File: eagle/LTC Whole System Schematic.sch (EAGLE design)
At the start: 22 parts

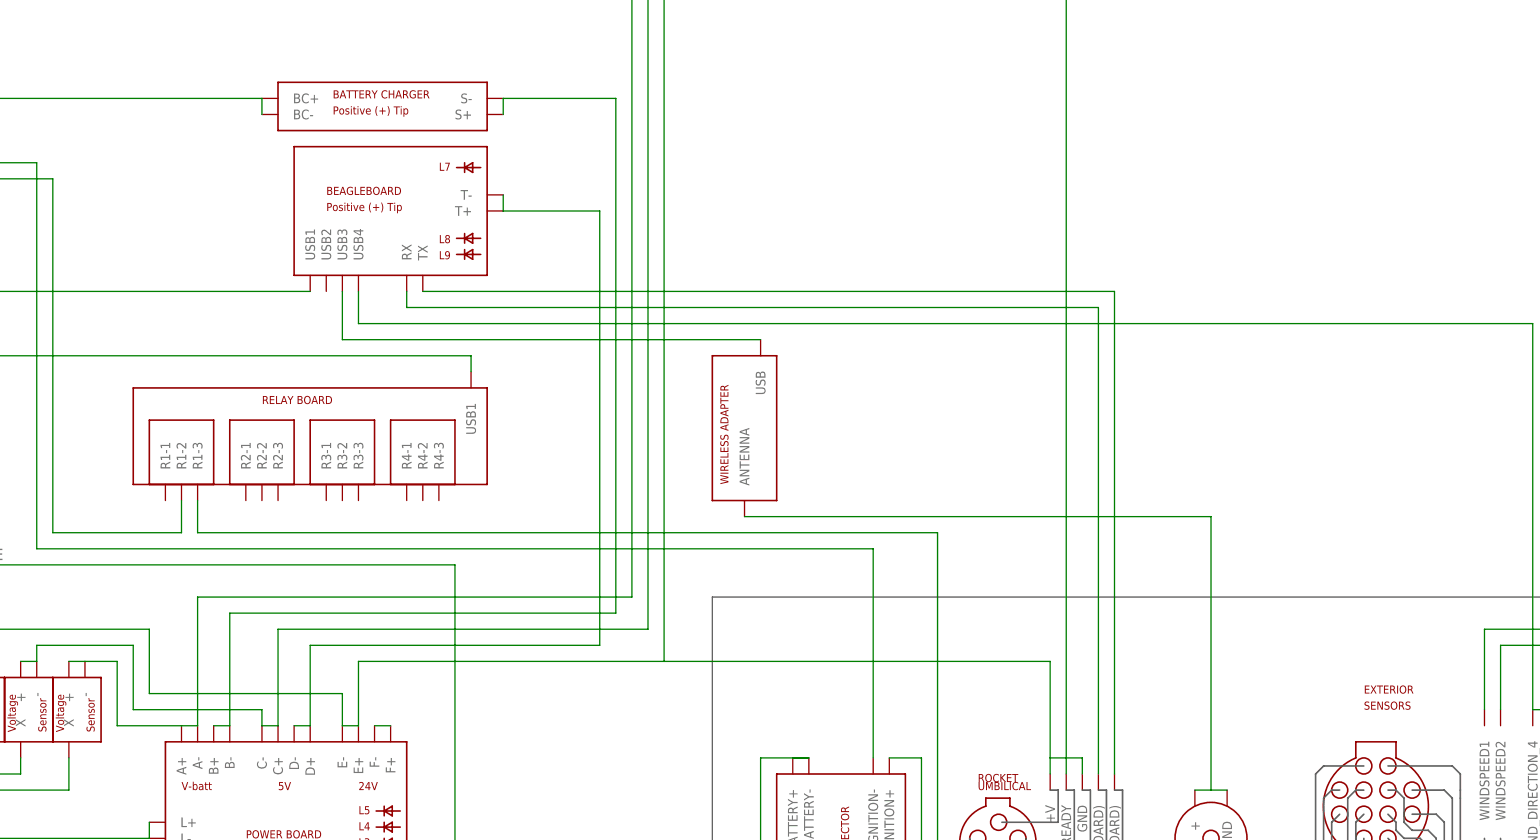
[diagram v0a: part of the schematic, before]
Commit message: Updated LV2 system schematic to include DC-DC adapter and extra relay connections.
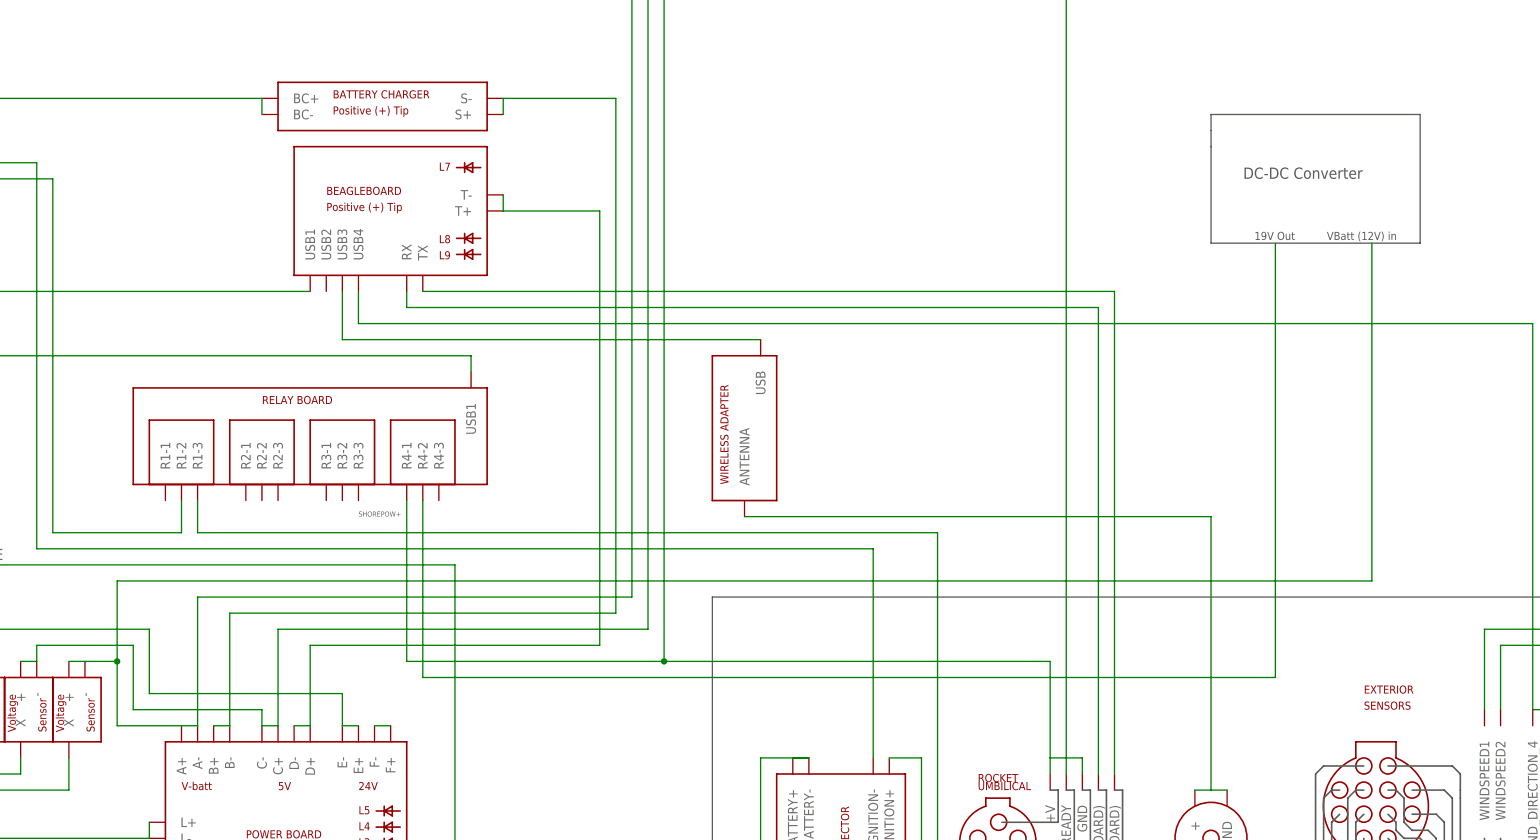
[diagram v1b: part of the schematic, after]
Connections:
- new net N$11: U$1.E+, U$1.E-, U$10.+, U$10.-
- new net SHOREPOW+: U$14.+V, U$14.GND, U$2.R+, U$6.R4-1
- net N$6: now also U$6.R4-2; no longer U$1.E+, U$1.E-, U$10.+, U$10.-, U$14.+V, U$14.GND, U$2.R+
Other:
- note added: "19V Out"
- note added: "DC-DC Converter"
- note added: "VBatt (12V) in"
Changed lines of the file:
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@@
 <?xml version="1.0" encoding="utf-8"?>
 <!DOCTYPE eagle SYSTEM "eagle.dtd">
-<eagle version="6.4">
+<eagle version="6.5.0">
 <drawing>
 <settings>
@@
 <text x="-54.356" y="-43.942" size="1.778" layer="92">SIDE PANEL</text>
 <text x="202.692" y="-51.562" size="1.778" layer="92">BOTTOM PANEL</text>
+<wire x1="210.82" y1="91.44" x2="210.82" y2="88.9" width="0.1524" layer="97"/>
+<wire x1="210.82" y1="88.9" x2="210.82" y2="73.66" width="0.1524" layer="97"/>
+<wire x1="210.82" y1="73.66" x2="243.84" y2="73.66" width="0.1524" layer="97"/>
+<wire x1="243.84" y1="73.66" x2="243.84" y2="93.98" width="0.1524" layer="97"/>
+<wire x1="243.84" y1="93.98" x2="210.82" y2="93.98" width="0.1524" layer="97"/>
+<wire x1="210.82" y1="93.98" x2="210.82" y2="91.44" width="0.1524" layer="97"/>
+<text x="215.9" y="83.82" size="1.778" layer="97">DC-DC Converter</text>
+<text x="217.678" y="74.168" size="1.27" layer="97">19V Out</text>
+<text x="229.108" y="74.168" size="1.27" layer="97">VBatt (12V) in</text>
 </plain>
 <instances>
@@
 <wire x1="38.1" y1="7.62" x2="38.1" y2="-2.54" width="0.2032" layer="91"/>
 <wire x1="38.1" y1="-2.54" x2="48.26" y2="-2.54" width="0.2032" layer="91"/>
+<wire x1="38.1" y1="7.62" x2="38.1" y2="20.32" width="0.1524" layer="91"/>
+<junction x="38.1" y="7.62"/>
+<wire x1="38.1" y1="20.32" x2="236.22" y2="20.32" width="0.1524" layer="91"/>
+<wire x1="236.22" y1="20.32" x2="236.22" y2="73.66" width="0.1524" layer="91"/>
 </segment>
 </net>
@@
 </segment>
 </net>
-<net name="N$6" class="0">
-<segment>
-<pinref part="U$10" gate="G$1" pin="-"/>
-<pinref part="U$10" gate="G$1" pin="+"/>
-<wire x1="15.24" y1="7.62" x2="17.78" y2="7.62" width="0.2032" layer="91"/>
-<wire x1="17.78" y1="7.62" x2="17.78" y2="12.7" width="0.2032" layer="91"/>
-<wire x1="17.78" y1="12.7" x2="43.18" y2="12.7" width="0.2032" layer="91"/>
-<wire x1="43.18" y1="12.7" x2="43.18" y2="2.54" width="0.2032" layer="91"/>
-<pinref part="U$1" gate="G$1" pin="E-"/>
-<pinref part="U$1" gate="G$1" pin="E+"/>
-<wire x1="73.66" y1="-2.54" x2="76.2" y2="-2.54" width="0.2032" layer="91"/>
-<wire x1="76.2" y1="-2.54" x2="76.2" y2="7.62" width="0.2032" layer="91"/>
-<wire x1="76.2" y1="7.62" x2="124.46" y2="7.62" width="0.2032" layer="91"/>
+<net name="SHOREPOW+" class="0">
+<segment>
 <wire x1="124.46" y1="7.62" x2="185.42" y2="7.62" width="0.2032" layer="91"/>
 <wire x1="185.42" y1="7.62" x2="185.42" y2="-7.62" width="0.2032" layer="91"/>
-<wire x1="43.18" y1="2.54" x2="73.66" y2="2.54" width="0.2032" layer="91"/>
-<wire x1="73.66" y1="2.54" x2="73.66" y2="-2.54" width="0.2032" layer="91"/>
 <pinref part="U$14" gate="G$1" pin="GND"/>
 <wire x1="190.5" y1="-10.16" x2="190.5" y2="-7.62" width="0.2032" layer="91"/>
@@
 <pinref part="U$2" gate="G$1" pin="R+"/>
 <wire x1="-35.56" y1="91.44" x2="-27.94" y2="91.44" width="0.2032" layer="91"/>
+<wire x1="124.46" y1="7.62" x2="86.36" y2="7.62" width="0.2032" layer="91"/>
+<junction x="124.46" y="7.62"/>
+<wire x1="86.36" y1="7.62" x2="83.82" y2="7.62" width="0.1524" layer="91"/>
+<pinref part="U$6" gate="G$1" pin="R4-1"/>
+<wire x1="83.82" y1="7.62" x2="83.82" y2="33.02" width="0.1524" layer="91"/>
+<label x="76.2" y="30.48" size="0.8128" layer="95"/>
 </segment>
 </net>
@@
 </segment>
 </net>
+<net name="N$11" class="0">
+<segment>
+<pinref part="U$1" gate="G$1" pin="E+"/>
+<pinref part="U$1" gate="G$1" pin="E-"/>
+<wire x1="73.66" y1="-2.54" x2="76.2" y2="-2.54" width="0.2032" layer="91"/>
+<wire x1="73.66" y1="2.54" x2="73.66" y2="-2.54" width="0.2032" layer="91"/>
+<wire x1="43.18" y1="2.54" x2="73.66" y2="2.54" width="0.2032" layer="91"/>
+<wire x1="43.18" y1="12.7" x2="43.18" y2="2.54" width="0.2032" layer="91"/>
+<wire x1="17.78" y1="12.7" x2="43.18" y2="12.7" width="0.2032" layer="91"/>
+<pinref part="U$10" gate="G$1" pin="-"/>
+<wire x1="17.78" y1="7.62" x2="17.78" y2="12.7" width="0.2032" layer="91"/>
+<pinref part="U$10" gate="G$1" pin="+"/>
+<wire x1="15.24" y1="7.62" x2="17.78" y2="7.62" width="0.2032" layer="91"/>
+</segment>
+</net>
+<net name="N$6" class="0">
+<segment>
+<pinref part="U$6" gate="G$1" pin="R4-2"/>
+<wire x1="86.36" y1="33.02" x2="86.36" y2="5.08" width="0.1524" layer="91"/>
+<wire x1="86.36" y1="5.08" x2="220.98" y2="5.08" width="0.1524" layer="91"/>
+<wire x1="220.98" y1="5.08" x2="220.98" y2="73.66" width="0.1524" layer="91"/>
+</segment>
+</net>
